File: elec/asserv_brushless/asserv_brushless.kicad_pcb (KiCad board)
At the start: 2 copper layers, 88 x 55 mm, 61 parts, among them J1 Conn_01x02, J2 Conn_01x04, J3 Conn_01x04, J4 Molex, J5 Molex, U1 Nucleo-F303K8, U2 L6235D, U3 L6235D

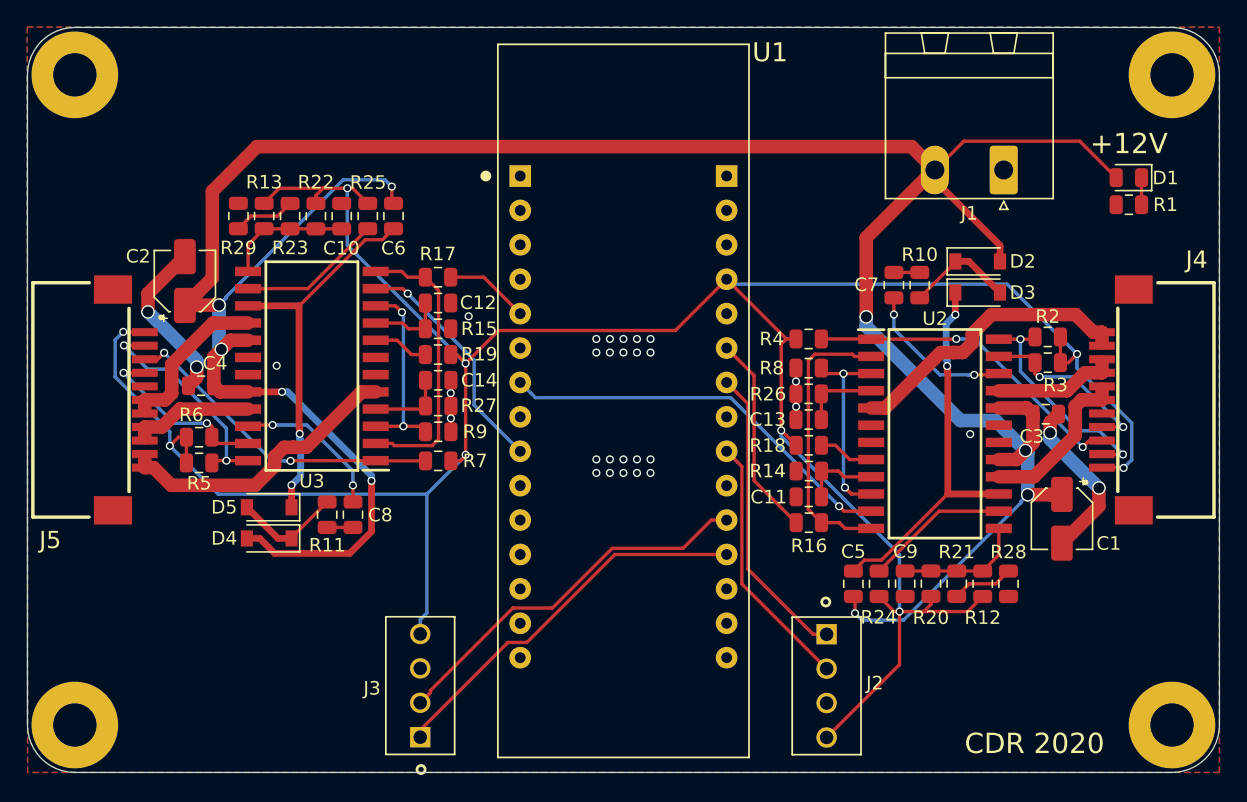
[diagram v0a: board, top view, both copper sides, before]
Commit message: changing cut out
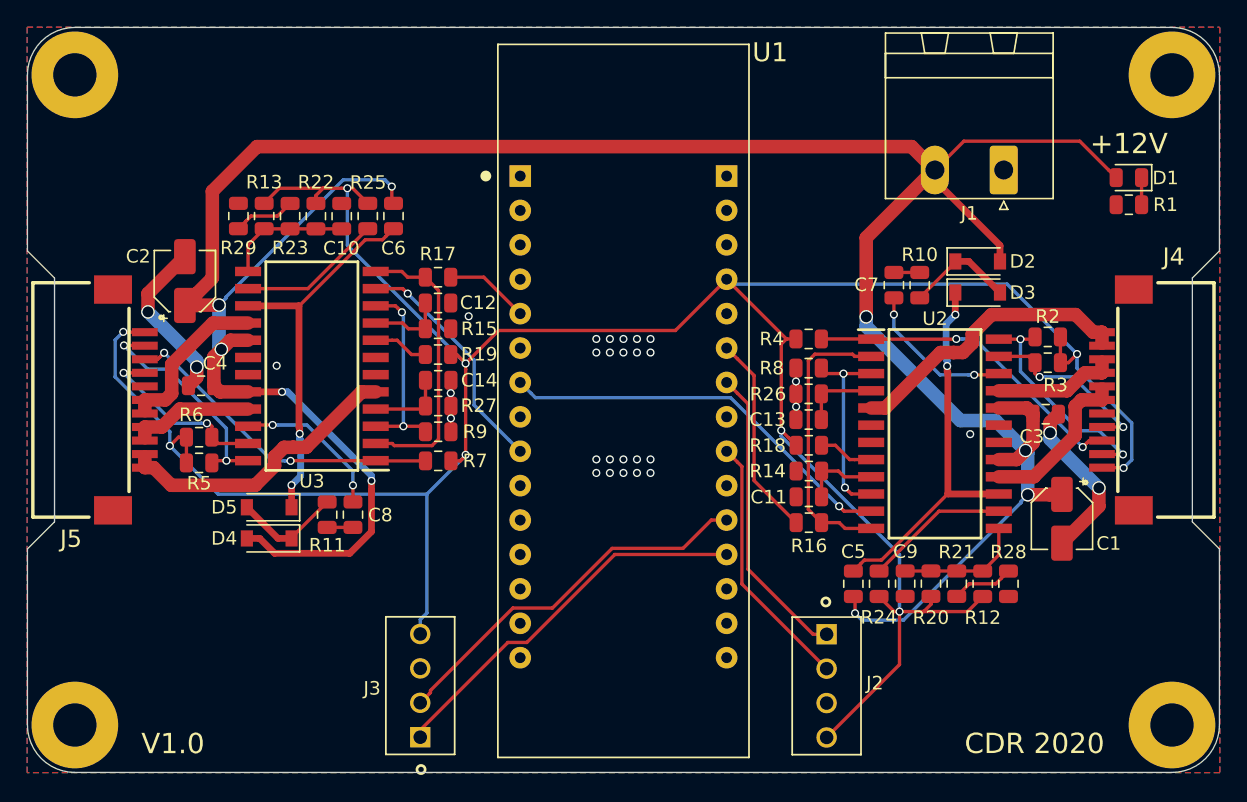
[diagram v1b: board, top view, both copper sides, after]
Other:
- outline, holes or cut-outs redrawn
- board text added: "V1.0"
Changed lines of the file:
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@@
   (general
     (thickness 1.6)
-    (drawings 14)
+    (drawings 23)
     (tracks 536)
     (zones 0)
@@
     (tags Connector)
     (attr smd)
-    (fp_text reference J4 (at 18.9992 5.8166 180) (layer F.SilkS)
+    (fp_text reference J4 (at 19.221 4.12 180) (layer F.SilkS)
       (effects (font (size 1.27 1.27) (thickness 0.254)))
     )
@@
     (tags Connector)
     (attr smd)
-    (fp_text reference J5 (at 18.9992 5.8166 180) (layer F.SilkS)
+    (fp_text reference J5 (at 18.907 4.287 180) (layer F.SilkS)
       (effects (font (size 1.27 1.27) (thickness 0.254)))
     )
@@
     )
   )
+  (gr_text V1.0 (at 60.7441 102.8827) (layer F.SilkS)
+    (effects (font (size 1.5 1.5) (thickness 0.3)))
+  )
+  (gr_line (start 138 66.5) (end 138 53.5) (layer Edge.Cuts) (width 0.05))
+  (gr_line (start 138 66.5) (end 136 68.5) (layer Edge.Cuts) (width 0.05))
+  (gr_line (start 138 88.5) (end 136 86.5) (layer Edge.Cuts) (width 0.05))
+  (gr_line (start 136 86.5) (end 136 68.5) (layer Edge.Cuts) (width 0.05))
+  (gr_line (start 50 88.5) (end 50 101.5) (layer Edge.Cuts) (width 0.05))
+  (gr_line (start 50 88.5) (end 52 86.5) (layer Edge.Cuts) (width 0.05))
+  (gr_line (start 52 68.5) (end 52 86.5) (layer Edge.Cuts) (width 0.05))
+  (gr_line (start 50 66.5) (end 52 68.5) (layer Edge.Cuts) (width 0.05))
   (dimension 81 (width 0.15) (layer Dwgs.User)
     (gr_text "81.000 mm" (at 94 111.099999) (layer Dwgs.User)
@@
     (arrow2b (pts (xy 50 40.894) (xy 51.126504 40.307579)))
   )
-  (gr_line (start 50 53.5) (end 50 101.5) (layer Edge.Cuts) (width 0.05))
+  (gr_line (start 50 53.5) (end 50 66.5) (layer Edge.Cuts) (width 0.05))
   (gr_line (start 53.5 105) (end 134.5 105) (layer Edge.Cuts) (width 0.05))
-  (gr_line (start 138 53.5) (end 138 101.5) (layer Edge.Cuts) (width 0.05))
+  (gr_line (start 138 88.5) (end 138 101.5) (layer Edge.Cuts) (width 0.05))
   (gr_line (start 53.5 50) (end 134.5 50) (layer Edge.Cuts) (width 0.05))
   (segment (start 81.2625 82) (end 81.97 82) (width 0.25) (layer F.Cu) (net 1))
@@
     (connect_pads (clearance 0.254))
     (min_thickness 0.254)
-    (fill yes (arc_segments 32) (thermal_gap 0.254) (thermal_bridge_width 0.508))
+    (fill yes (arc_segments 32) (thermal_gap 0.508) (thermal_bridge_width 0.508))
     (polygon
       (pts
-        (xy 49.9872 49.9872) (xy 137.9982 49.9872) (xy 137.9982 105.0036) (xy 50.0126 105.0036)
+        (xy 49.9745 49.9872) (xy 138.0236 49.9872) (xy 138.0236 105.0163) (xy 49.9745 105.0163)
       )
     )
@@
     (connect_pads (clearance 0.254))
     (min_thickness 0.254)
-    (fill yes (arc_segments 32) (thermal_gap 0.254) (thermal_bridge_width 0.508))
+    (fill yes (arc_segments 32) (thermal_gap 0.508) (thermal_bridge_width 0.508))
     (polygon
       (pts
-        (xy 49.987126 49.9872) (xy 137.998126 49.9872) (xy 137.998126 105.0036) (xy 50.012526 105.0036)
+        (xy 49.9745 49.9872) (xy 138.0236 49.9872) (xy 138.0236 105.0163) (xy 49.9745 105.0163)
       )
     )

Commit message: Add step file
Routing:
- net GND: track 28.6 -> 44.1 mm
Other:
- board text added: "Brushless Motors V1.0"
- board text removed: "V1.0"
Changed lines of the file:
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@@
     (thickness 1.6)
     (drawings 23)
-    (tracks 536)
+    (tracks 540)
     (zones 0)
     (modules 61)
@@
     )
   )
-  (gr_text V1.0 (at 60.7441 102.8827) (layer F.SilkS)
+  (gr_text "Brushless Motors V1.0" (at 70.8152 52.451) (layer F.SilkS)
     (effects (font (size 1.5 1.5) (thickness 0.3)))
   )
@@
   (via (at 96 73) (size 0.6) (drill 0.4) (layers F.Cu B.Cu) (net 4))
   (via (at 96 74) (size 0.6) (drill 0.4) (layers F.Cu B.Cu) (net 4))
+  (segment (start 85.580001 67.790001) (end 86.38 68.59) (width 0.25) (layer F.Cu) (net 4))
+  (segment (start 81.83999 64.04999) (end 85.580001 67.790001) (width 0.25) (layer F.Cu) (net 4))
+  (segment (start 74.25509 64.04999) (end 81.83999 64.04999) (width 0.25) (layer F.Cu) (net 4))
+  (segment (start 73.2014 62.9963) (end 74.25509 64.04999) (width 0.25) (layer F.Cu) (net 4))
   (via (at 118.506247 71.206253) (size 0.6) (drill 0.4) (layers F.Cu B.Cu) (net 22))
   (segment (start 111.78751 89.32499) (end 111.531237 89.581263) (width 0.25) (layer F.Cu) (net 22))
